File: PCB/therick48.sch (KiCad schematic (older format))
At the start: 132 parts, among them J1 TYPE-C-31-M12_13, J2 AVR-ISP-6_mod, K1 KEYSW, K10 KEYSW, K11 KEYSW, K12 KEYSW, K13 KEYSW, K14 KEYSW, K15 KEYSW, K16 KEYSW, K17 KEYSW, K18 KEYSW, K19 KEYSW, K2 KEYSW, K20 KEYSW, K21 KEYSW, K22 KEYSW, K23 KEYSW, K24 KEYSW, K25 KEYSW, K26 KEYSW, K27 KEYSW, K28 KEYSW, K29 KEYSW, K3 KEYSW, K30 KEYSW, K31 KEYSW, K32 KEYSW, K33 KEYSW, K34 KEYSW, K35 KEYSW, K36 KEYSW, K37 KEYSW, K38 KEYSW, K39 KEYSW, K4 KEYSW, K40 KEYSW, K41 KEYSW, K42 KEYSW, K43 KEYSW, K44 KEYSW, K45 KEYSW, K46 KEYSW, K47 KEYSW, K48 KEYSW, K5 KEYSW, K6 KEYSW, K7 KEYSW, K8 KEYSW, K9 KEYSW, SW1 SW_PUSH, U1 ATMEGA32U4, U2 HOLE, U3 USBLC6-2SC6, Y1 16MHz

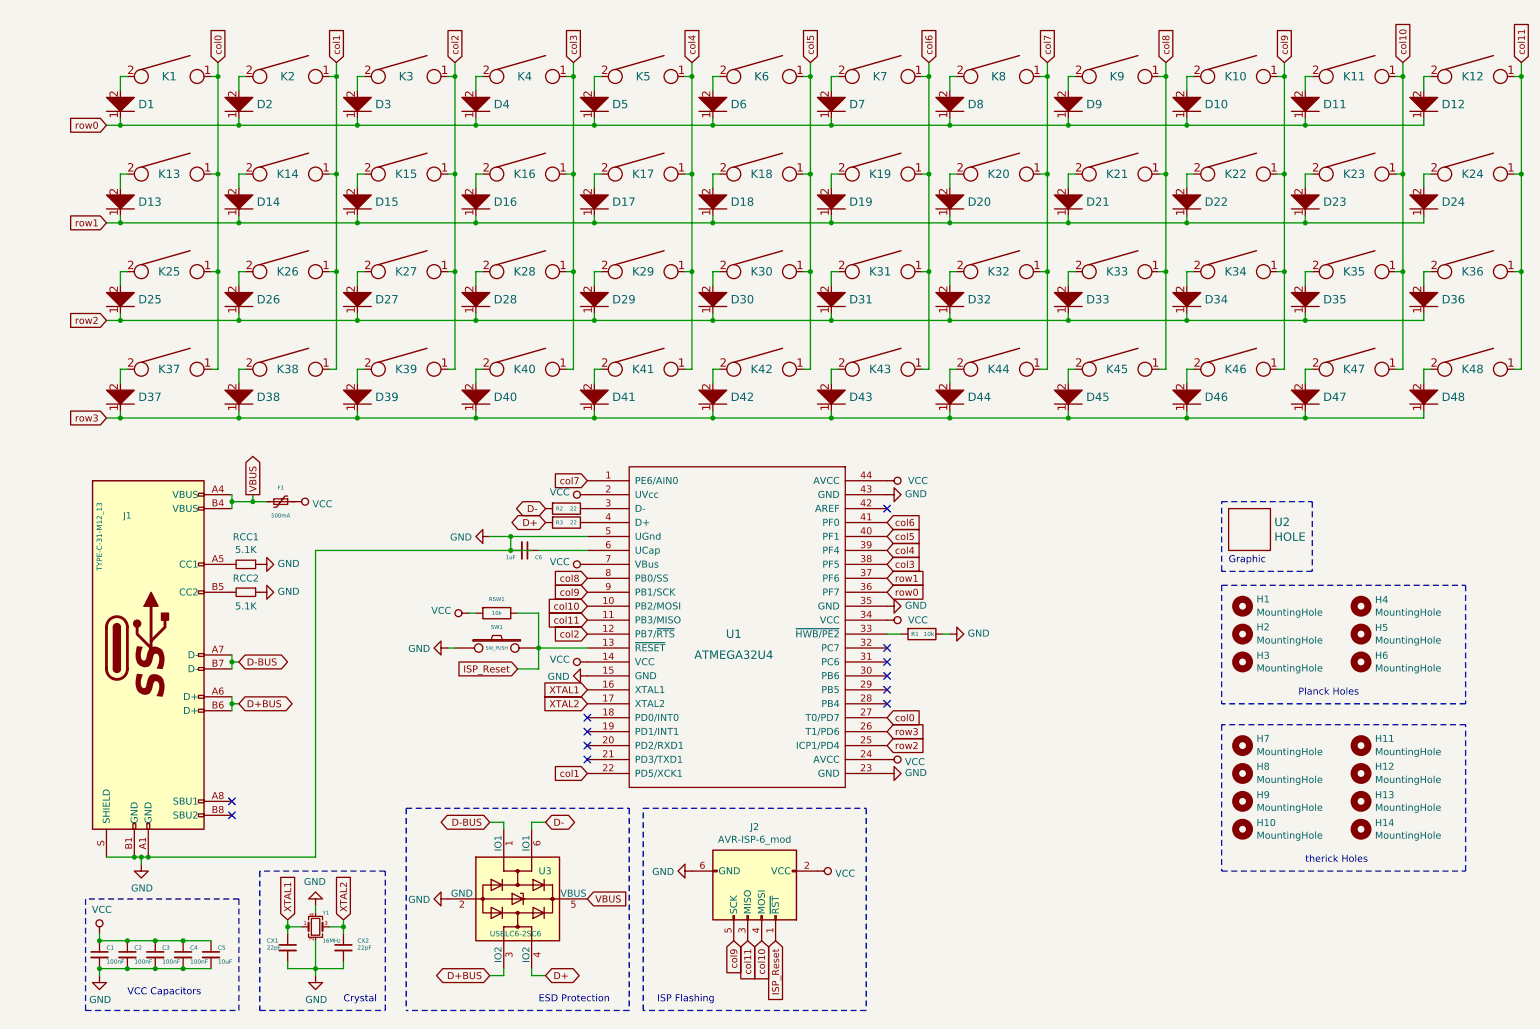
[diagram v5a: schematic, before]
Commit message: Move mounting holes to PCB
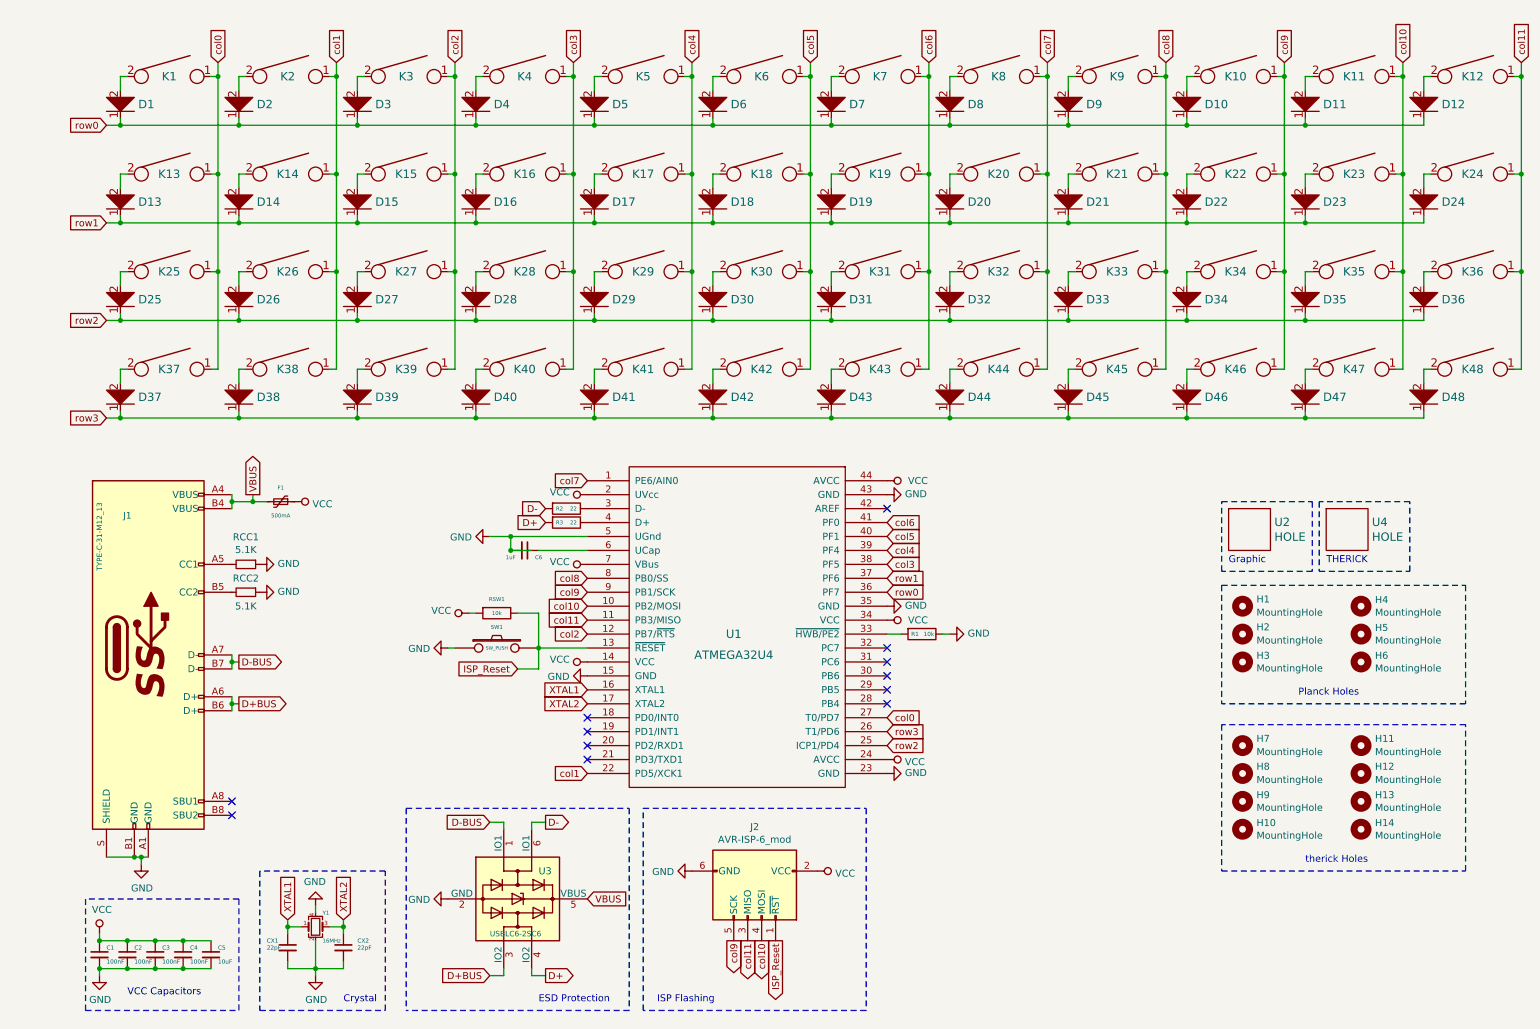
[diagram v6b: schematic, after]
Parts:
- added U4: HOLE, Artwork:THERICK, symbol lets_split-cache:HOLE
- H1, H10, H11, H12, H13, H14, H2, H3, H4, H5, H6, H7, H8, H9: footprint random-keyboard-parts:plate_hole_4mm_tht -> random-keyboard-parts:Generic-Mounthole
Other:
- note added: "THERICK"
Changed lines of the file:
@@
 F 0 "H1" H 9350 4850 50  0000 L CNN
 F 1 "MountingHole" H 9350 4755 50  0000 L CNN
-F 2 "random-keyboard-parts:plate_hole_4mm_tht" H 9250 4800 50  0001 C CNN
+F 2 "random-keyboard-parts:Generic-Mounthole" H 9250 4800 50  0001 C CNN
 F 3 "~" H 9250 4800 50  0001 C CNN
 	1    9250 4800
@@
 F 0 "H3" H 9350 5246 50  0000 L CNN
 F 1 "MountingHole" H 9350 5155 50  0000 L CNN
-F 2 "random-keyboard-parts:plate_hole_4mm_tht" H 9250 5200 50  0001 C CNN
+F 2 "random-keyboard-parts:Generic-Mounthole" H 9250 5200 50  0001 C CNN
 F 3 "~" H 9250 5200 50  0001 C CNN
 	1    9250 5200
@@
 F 0 "H4" H 10200 4846 50  0000 L CNN
 F 1 "MountingHole" H 10200 4755 50  0000 L CNN
-F 2 "random-keyboard-parts:plate_hole_4mm_tht" H 10100 4800 50  0001 C CNN
+F 2 "random-keyboard-parts:Generic-Mounthole" H 10100 4800 50  0001 C CNN
 F 3 "~" H 10100 4800 50  0001 C CNN
 	1    10100 4800
@@
 F 0 "H5" H 10200 5046 50  0000 L CNN
 F 1 "MountingHole" H 10200 4955 50  0000 L CNN
-F 2 "random-keyboard-parts:plate_hole_4mm_tht" H 10100 5000 50  0001 C CNN
+F 2 "random-keyboard-parts:Generic-Mounthole" H 10100 5000 50  0001 C CNN
 F 3 "~" H 10100 5000 50  0001 C CNN
 	1    10100 5000
@@
 F 0 "H6" H 10200 5246 50  0000 L CNN
 F 1 "MountingHole" H 10200 5155 50  0000 L CNN
-F 2 "random-keyboard-parts:plate_hole_4mm_tht" H 10100 5200 50  0001 C CNN
+F 2 "random-keyboard-parts:Generic-Mounthole" H 10100 5200 50  0001 C CNN
 F 3 "~" H 10100 5200 50  0001 C CNN
 	1    10100 5200
@@
 Wire Notes Line
 	9750 4550 9100 4550
-Text GLabel 2050 5500 2    50   BiDi ~ 0
+Text GLabel 2050 5500 2    50   Output ~ 0
 D+BUS
-Text GLabel 2050 5200 2    50   BiDi ~ 0
+Text GLabel 2050 5200 2    50   Output ~ 0
 D-BUS
 Text GLabel 6700 4600 2    50   Input ~ 0
@@
 	2800 7100 2800 7050
 Connection ~ 2800 7100
-Text GLabel 4250 7450 2    50   BiDi ~ 0
+Text GLabel 4250 7450 2    50   Output ~ 0
 D+
-Text GLabel 3850 7450 0    50   BiDi ~ 0
+Text GLabel 3850 7450 0    50   Input ~ 0
 D+BUS
-Text GLabel 3850 6350 0    50   BiDi ~ 0
+Text GLabel 3850 6350 0    50   Input ~ 0
 D-BUS
-Text GLabel 4250 6350 2    50   BiDi ~ 0
+Text GLabel 4250 6350 2    50   Output ~ 0
 D-
 Wire Wire Line
@@
 	0    1    1    0
 $EndComp
-Text GLabel 4250 4200 0    50   BiDi ~ 0
+Text GLabel 4250 4200 0    50   Input ~ 0
 D+
-Text GLabel 4250 4100 0    50   BiDi ~ 0
+Text GLabel 4250 4100 0    50   Input ~ 0
 D-
 Text GLabel 6700 4500 2    50   Input ~ 0
@@
 F 0 "H2" H 9350 5050 50  0000 L CNN
 F 1 "MountingHole" H 9350 4955 50  0000 L CNN
-F 2 "random-keyboard-parts:plate_hole_4mm_tht" H 9250 5000 50  0001 C CNN
+F 2 "random-keyboard-parts:Generic-Mounthole" H 9250 5000 50  0001 C CNN
 F 3 "~" H 9250 5000 50  0001 C CNN
 	1    9250 5000
@@
 	0    1    1    0
 $EndComp
-Text GLabel 5800 7200 3    50   Input ~ 0
+Text GLabel 5800 7200 3    50   Output ~ 0
 col10
-Text GLabel 5700 7200 3    50   Input ~ 0
+Text GLabel 5700 7200 3    50   Output ~ 0
 col11
-Text GLabel 5600 7200 3    50   Input ~ 0
+Text GLabel 5600 7200 3    50   Output ~ 0
 col9
 $Comp
@@
 Text GLabel 4050 5250 0    50   Input ~ 0
 ISP_Reset
-Text GLabel 5900 7200 3    50   Input ~ 0
+Text GLabel 5900 7200 3    50   Output ~ 0
 ISP_Reset
 Text Notes 5050 7650 0    50   ~ 0
@@
 Wire Wire Line
 	1350 6600 1400 6600
-Connection ~ 1400 6600
 $Comp
 L acheronSymbols:TYPE-C-31-M12_13 J1
@@
 	1    0    0    -1
 $EndComp
-Wire Wire Line
-	2600 6600 2600 4400
-Wire Wire Line
-	1400 6600 2600 6600
-Wire Wire Line
-	2600 4400 4000 4400
 Wire Notes Line
 	9100 4650 10850 4650
@@
 F 0 "H7" H 9350 5850 50  0000 L CNN
 F 1 "MountingHole" H 9350 5755 50  0000 L CNN
-F 2 "random-keyboard-parts:plate_hole_4mm_tht" H 9250 5800 50  0001 C CNN
+F 2 "random-keyboard-parts:Generic-Mounthole" H 9250 5800 50  0001 C CNN
 F 3 "~" H 9250 5800 50  0001 C CNN
 	1    9250 5800
@@
 F 0 "H9" H 9350 6246 50  0000 L CNN
 F 1 "MountingHole" H 9350 6155 50  0000 L CNN
-F 2 "random-keyboard-parts:plate_hole_4mm_tht" H 9250 6200 50  0001 C CNN
+F 2 "random-keyboard-parts:Generic-Mounthole" H 9250 6200 50  0001 C CNN
 F 3 "~" H 9250 6200 50  0001 C CNN
 	1    9250 6200
@@
 F 0 "H10" H 9350 6446 50  0000 L CNN
 F 1 "MountingHole" H 9350 6355 50  0000 L CNN
-F 2 "random-keyboard-parts:plate_hole_4mm_tht" H 9250 6400 50  0001 C CNN
+F 2 "random-keyboard-parts:Generic-Mounthole" H 9250 6400 50  0001 C CNN
 F 3 "~" H 9250 6400 50  0001 C CNN
 	1    9250 6400
@@
 F 0 "H8" H 9350 6050 50  0000 L CNN
 F 1 "MountingHole" H 9350 5955 50  0000 L CNN
-F 2 "random-keyboard-parts:plate_hole_4mm_tht" H 9250 6000 50  0001 C CNN
+F 2 "random-keyboard-parts:Generic-Mounthole" H 9250 6000 50  0001 C CNN
 F 3 "~" H 9250 6000 50  0001 C CNN
 	1    9250 6000
@@
 F 0 "H11" H 10200 5850 50  0000 L CNN
 F 1 "MountingHole" H 10200 5755 50  0000 L CNN
-F 2 "random-keyboard-parts:plate_hole_4mm_tht" H 10100 5800 50  0001 C CNN
+F 2 "random-keyboard-parts:Generic-Mounthole" H 10100 5800 50  0001 C CNN
 F 3 "~" H 10100 5800 50  0001 C CNN
 	1    10100 5800
@@
 F 0 "H13" H 10200 6246 50  0000 L CNN
 F 1 "MountingHole" H 10200 6155 50  0000 L CNN
-F 2 "random-keyboard-parts:plate_hole_4mm_tht" H 10100 6200 50  0001 C CNN
+F 2 "random-keyboard-parts:Generic-Mounthole" H 10100 6200 50  0001 C CNN
 F 3 "~" H 10100 6200 50  0001 C CNN
 	1    10100 6200
@@
 F 0 "H14" H 10200 6446 50  0000 L CNN
 F 1 "MountingHole" H 10200 6355 50  0000 L CNN
-F 2 "random-keyboard-parts:plate_hole_4mm_tht" H 10100 6400 50  0001 C CNN
+F 2 "random-keyboard-parts:Generic-Mounthole" H 10100 6400 50  0001 C CNN
 F 3 "~" H 10100 6400 50  0001 C CNN
 	1    10100 6400
@@
 F 0 "H12" H 10200 6050 50  0000 L CNN
 F 1 "MountingHole" H 10200 5955 50  0000 L CNN
-F 2 "random-keyboard-parts:plate_hole_4mm_tht" H 10100 6000 50  0001 C CNN
+F 2 "random-keyboard-parts:Generic-Mounthole" H 10100 6000 50  0001 C CNN
 F 3 "~" H 10100 6000 50  0001 C CNN
 	1    10100 6000
@@
 	0    1    1    0
 $EndComp
+$Comp
+L lets_split-cache:HOLE U4
+U 1 1 5EC53EDB
+P 10000 4250
+F 0 "U4" H 10178 4303 60  0000 L CNN
+F 1 "HOLE" H 10178 4197 60  0000 L CNN
+F 2 "Artwork:THERICK" H 10000 4250 60  0001 C CNN
+F 3 "" H 10000 4250 60  0001 C CNN
+	1    10000 4250
+	1    0    0    -1
+$EndComp
+Text Notes 9850 4500 0    50   ~ 0
+THERICK
+Wire Notes Line
+	9800 4050 9800 4550
+Wire Notes Line
+	9800 4550 10450 4550
+Wire Notes Line
+	10450 4550 10450 4050
+Wire Notes Line
+	10450 4050 9800 4050
 $EndSCHEMATC
